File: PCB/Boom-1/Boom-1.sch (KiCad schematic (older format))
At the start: 698 parts

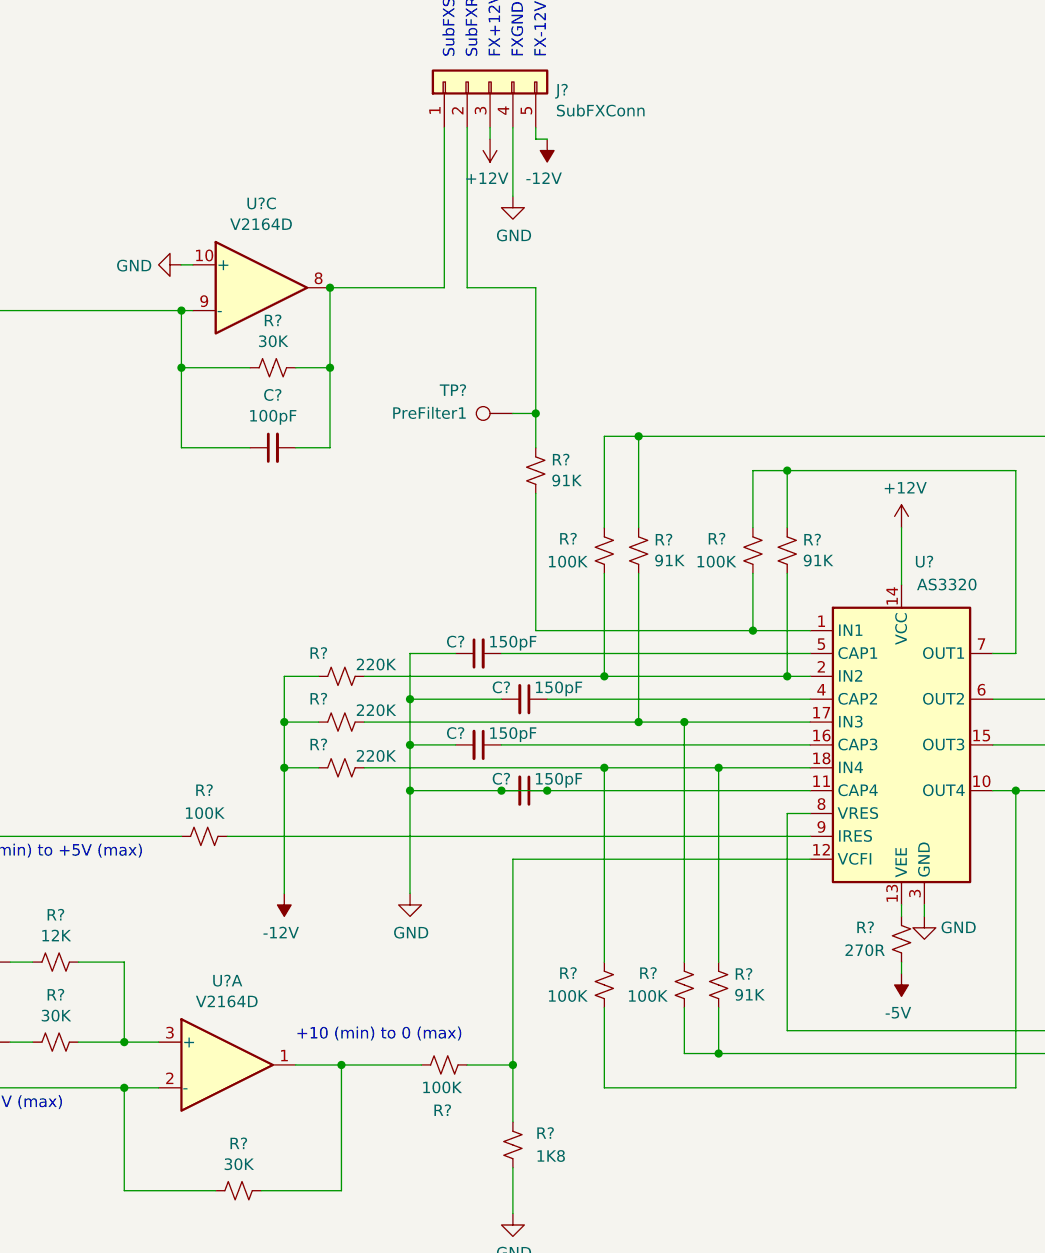
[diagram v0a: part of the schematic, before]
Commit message: replaced tl072 in sub osc filt
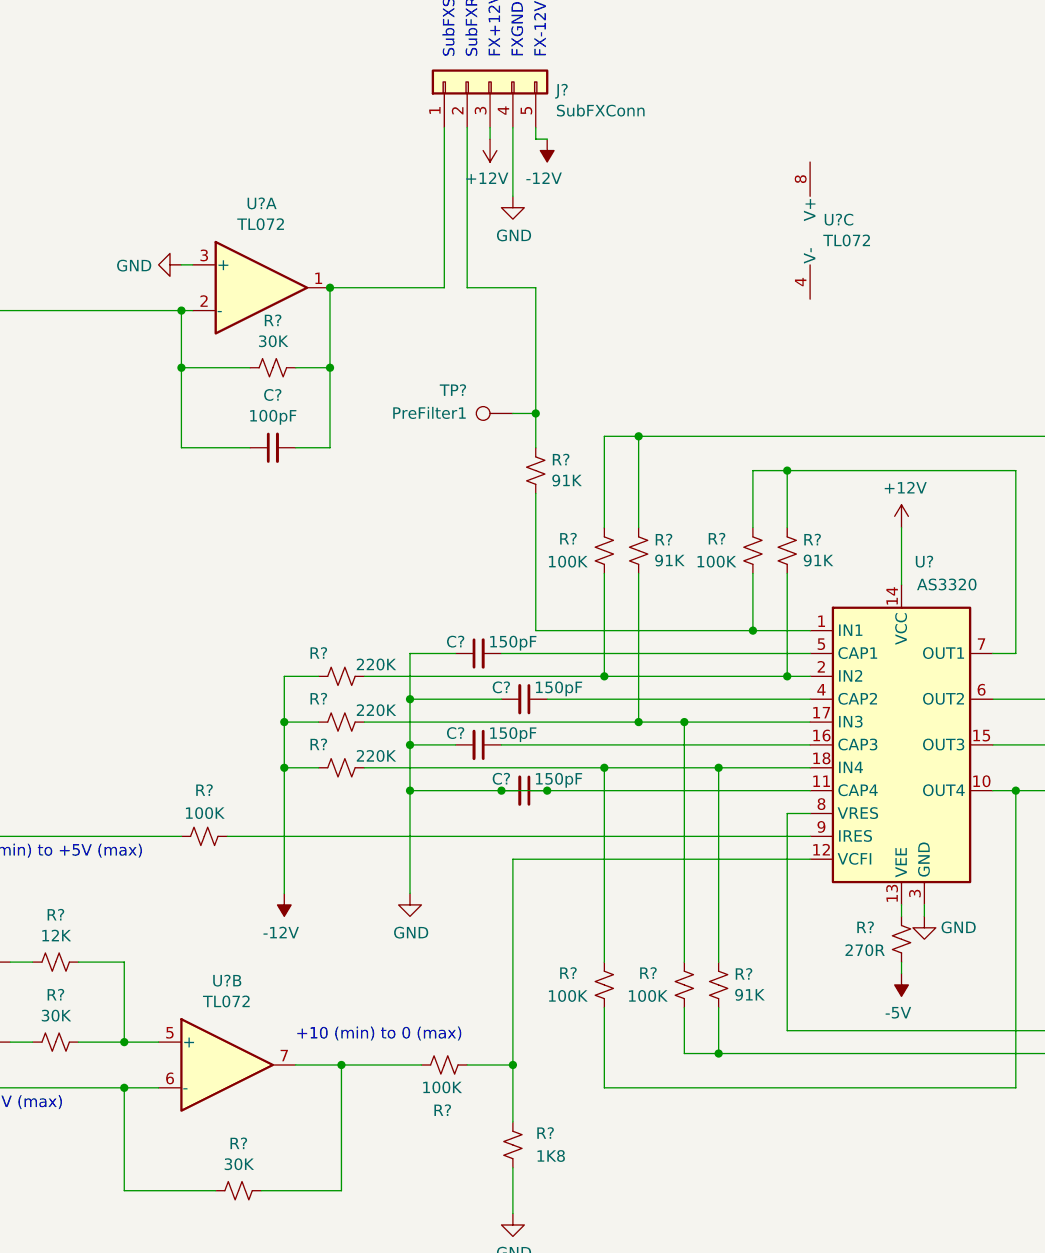
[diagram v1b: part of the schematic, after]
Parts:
- removed U? (x2): V2164D, Package_DIP:DIP-16_W7.62mm_Socket, symbol Amplifier_Operational:TL074
- added U? (x3): TL072, symbol Amplifier_Operational:TL072
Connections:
- net GND: now also U?.3 (+)
- net at C?.1, R?.2, U?.5 (Io2)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: now also U?.2 (-)
- net at C?.2, J?.1 (Pin_1), R?.1: now also U?.1
- net at R?.1, R?.2, R?.2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: now also U?.6 (-)
- net at R?.1, R?.2: now also U?.7
- net at R?.1, R?.1: now also U?.5 (+)
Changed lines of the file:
@@
 Wire Wire Line
 	22550 40500 26350 40500
-Connection ~ 18700 38300
 Wire Wire Line
 	16350 42300 16350 45400
@@
 $Comp
 L Amplifier_Operational:TL074 U?
-U 3 1 607506FD
-P 18400 38300
-F 0 "U?" H 18400 38667 50  0000 C CNN
-F 1 "V2164D" H 18400 38576 50  0000 C CNN
-F 2 "Package_DIP:DIP-16_W7.62mm_Socket" H 18350 38400 50  0001 C CNN
-F 3 "" H 18450 38500 50  0001 C CNN
-	3    18400 38300
-	1    0    0    -1
-$EndComp
-$Comp
-L Amplifier_Operational:TL074 U?
 U 1 1 5EA62AE2
 P 7100 44950
@@
 $Comp
 L Amplifier_Operational:TL074 U?
-U 1 1 6CFE24C1
-P 18250 41700
-F 0 "U?" H 18250 42067 50  0000 C CNN
-F 1 "V2164D" H 18250 41976 50  0000 C CNN
-F 2 "Package_DIP:DIP-16_W7.62mm_Socket" H 18200 41800 50  0001 C CNN
-F 3 "" H 18300 41900 50  0001 C CNN
-	1    18250 41700
-	1    0    0    -1
-$EndComp
-$Comp
-L Amplifier_Operational:TL074 U?
 U 1 1 89F24323
 P 31500 37000
@@
 	1    0    0    -1
 $EndComp
+$Comp
+L Amplifier_Operational:TL072 U?
+U 1 1 690F5BAC
+P 18400 38300
+F 0 "U?" H 18400 38667 50  0000 C CNN
+F 1 "TL072" H 18400 38576 50  0000 C CNN
+F 2 "" H 18400 38300 50  0001 C CNN
+F 3 "http://www.ti.com/lit/ds/symlink/tl071.pdf" H 18400 38300 50  0001 C CNN
+	1    18400 38300
+	1    0    0    -1
+$EndComp
+Connection ~ 18700 38300
+$Comp
+L Amplifier_Operational:TL072 U?
+U 2 1 690FE8E2
+P 18250 41700
+F 0 "U?" H 18250 42067 50  0000 C CNN
+F 1 "TL072" H 18250 41976 50  0000 C CNN
+F 2 "" H 18250 41700 50  0001 C CNN
+F 3 "http://www.ti.com/lit/ds/symlink/tl071.pdf" H 18250 41700 50  0001 C CNN
+	2    18250 41700
+	1    0    0    -1
+$EndComp
+$Comp
+L Amplifier_Operational:TL072 U?
+U 3 1 69108260
+P 20900 38050
+F 0 "U?" H 20858 38096 50  0000 L CNN
+F 1 "TL072" H 20858 38005 50  0000 L CNN
+F 2 "" H 20900 38050 50  0001 C CNN
+F 3 "http://www.ti.com/lit/ds/symlink/tl071.pdf" H 20900 38050 50  0001 C CNN
+	3    20900 38050
+	1    0    0    -1
+$EndComp

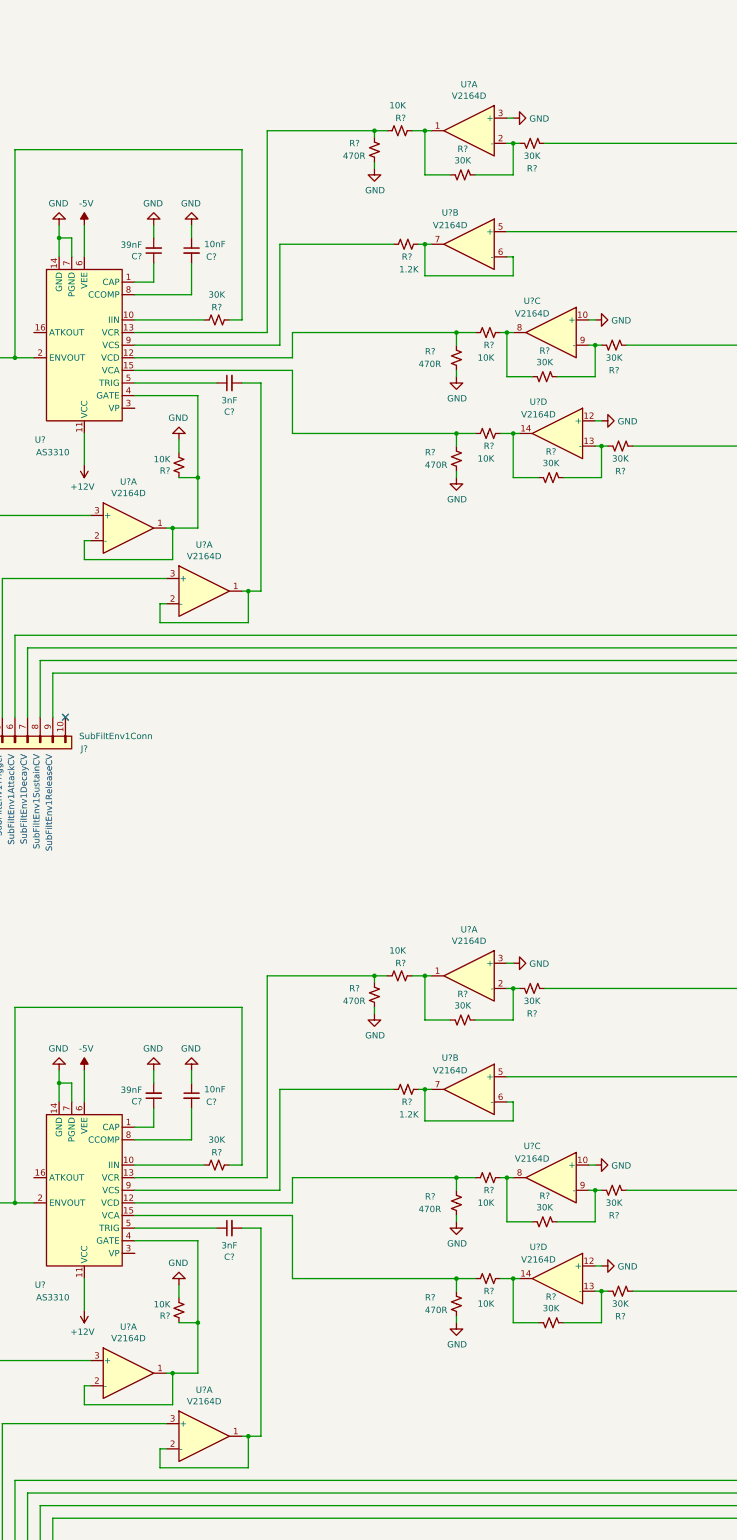
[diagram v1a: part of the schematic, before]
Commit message: replaced TL074s in sub osc filt env 1 and 2
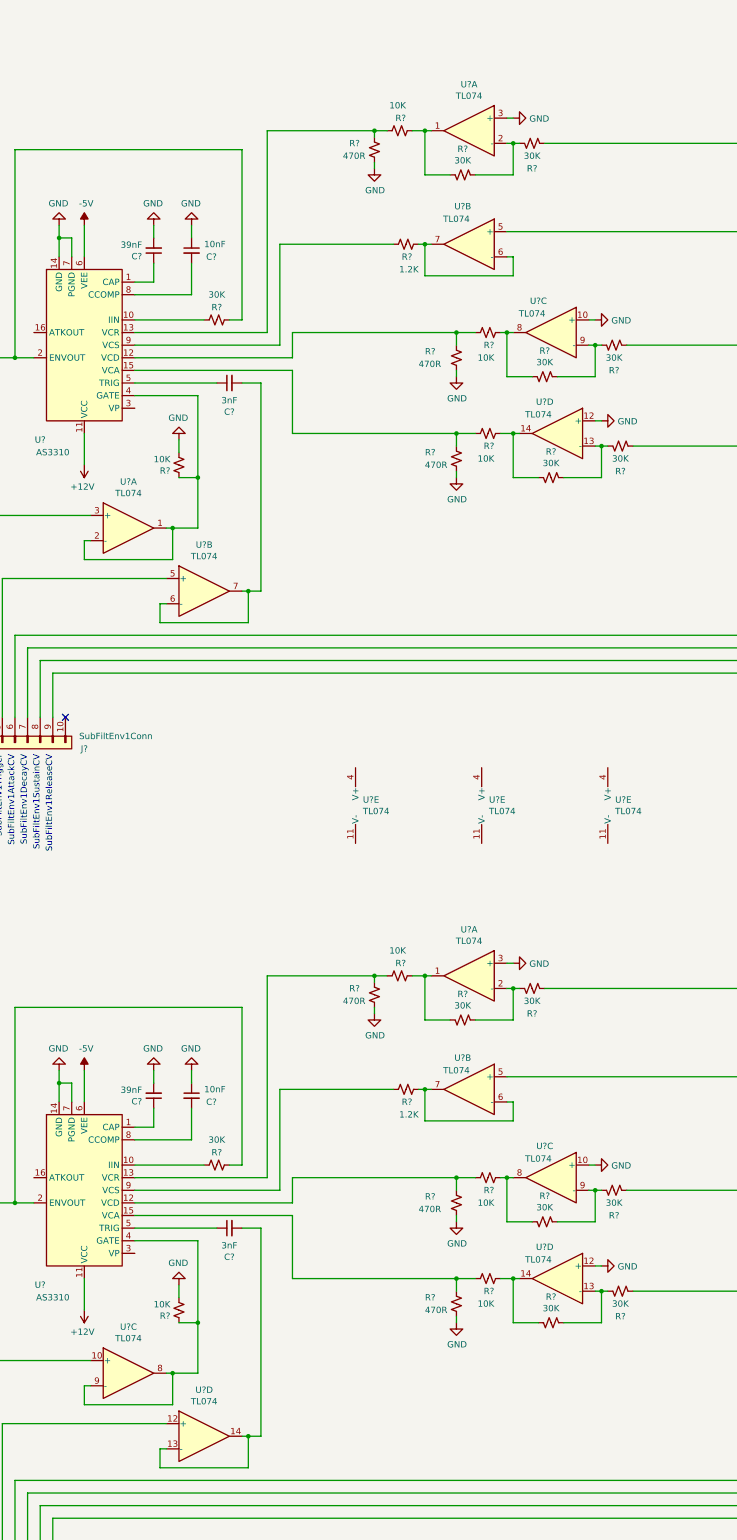
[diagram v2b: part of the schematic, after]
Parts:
- removed U? (x4): V2164D, Package_DIP:DIP-16_W7.62mm_Socket, symbol Amplifier_Operational:TL072
- removed U? (x8): V2164D, Package_DIP:DIP-16_W7.62mm_Socket, symbol Amplifier_Operational:TL074
- added U? (x15): TL074, symbol Amplifier_Operational:TL074
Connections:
- net GND: now also U?.10 (+), U?.10 (+), U?.12 (+), U?.12 (+), U?.3 (+), U?.3 (+)
- net at R?.1, U?.4 (GATE): now also U?.1, U?.2 (-)
- net at R?.1, U?.4 (GATE): now also U?.8, U?.9 (-)
- net at C?.2: now also U?.13 (-), U?.14
- net at C?.2: now also U?.6 (-), U?.7
- net at J?.4 (Pin_4): now also U?.3 (+)
- net at J?.5 (Pin_5): now also U?.5 (+)
- net at J?.4 (Pin_4): now also U?.10 (+)
- net at J?.5 (Pin_5): now also U?.12 (+)
- net at J?.8 (Pin_8): now also U?.5 (+) (x2)
- net at R?.1, R?.2: now also U?.1 (x2)
- net at R?.2: now also U?.6 (-), U?.7 (x2)
- net at R?.2, R?.2: now also U?.2 (-) (x2)
- net at R?.1, R?.2: now also U?.8 (x2)
- net at R?.2, R?.2: now also U?.9 (-) (x2)
- net at R?.1, R?.2: now also U?.14 (x2)
- net at R?.2, R?.2: now also U?.13 (-) (x2)
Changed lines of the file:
@@
 Wire Wire Line
 	22050 45700 22050 45750
-$Comp
-L Amplifier_Operational:TL074 U?
-U 2 1 8B0E7300
-P 22150 44700
-F 0 "U?" H 22300 44950 50  0000 C CNN
-F 1 "V2164D" H 22300 44850 50  0000 C CNN
-F 2 "Package_DIP:DIP-16_W7.62mm_Socket" H 22100 44800 50  0001 C CNN
-F 3 "" H 22200 44900 50  0001 C CNN
-	2    22150 44700
-	-1   0    0    -1
-$EndComp
 Wire Wire Line
 	21550 44700 20650 44700
@@
 Wire Wire Line
 	22050 52400 22050 52450
-$Comp
-L Amplifier_Operational:TL074 U?
-U 2 1 8BCFB81C
-P 22150 51400
-F 0 "U?" H 22300 51650 50  0000 C CNN
-F 1 "V2164D" H 22300 51550 50  0000 C CNN
-F 2 "Package_DIP:DIP-16_W7.62mm_Socket" H 22100 51500 50  0001 C CNN
-F 3 "" H 22200 51600 50  0001 C CNN
-	2    22150 51400
-	-1   0    0    -1
-$EndComp
 Wire Wire Line
 	21550 51400 20650 51400
@@
 $Comp
 L Amplifier_Operational:TL074 U?
-U 1 1 8B0E705B
-P 22150 43800
-F 0 "U?" H 22150 44167 50  0000 C CNN
-F 1 "V2164D" H 22150 44076 50  0000 C CNN
-F 2 "Package_DIP:DIP-16_W7.62mm_Socket" H 22100 43900 50  0001 C CNN
-F 3 "" H 22200 44000 50  0001 C CNN
-	1    22150 43800
-	-1   0    0    -1
-$EndComp
-$Comp
-L Amplifier_Operational:TL074 U?
-U 3 1 8B0E7151
-P 22800 45400
-F 0 "U?" H 22950 45650 50  0000 C CNN
-F 1 "V2164D" H 22950 45550 50  0000 C CNN
-F 2 "Package_DIP:DIP-16_W7.62mm_Socket" H 22750 45500 50  0001 C CNN
-F 3 "" H 22850 45600 50  0001 C CNN
-	3    22800 45400
-	-1   0    0    -1
-$EndComp
-$Comp
-L Amplifier_Operational:TL074 U?
-U 4 1 8B0E7247
-P 22850 46200
-F 0 "U?" H 23000 46450 50  0000 C CNN
-F 1 "V2164D" H 23000 46350 50  0000 C CNN
-F 2 "Package_DIP:DIP-16_W7.62mm_Socket" H 22800 46300 50  0001 C CNN
-F 3 "" H 22900 46400 50  0001 C CNN
-	4    22850 46200
-	-1   0    0    -1
-$EndComp
-$Comp
-L Amplifier_Operational:TL074 U?
-U 1 1 8BCFB577
-P 22150 50500
-F 0 "U?" H 22150 50867 50  0000 C CNN
-F 1 "V2164D" H 22150 50776 50  0000 C CNN
-F 2 "Package_DIP:DIP-16_W7.62mm_Socket" H 22100 50600 50  0001 C CNN
-F 3 "" H 22200 50700 50  0001 C CNN
-	1    22150 50500
-	-1   0    0    -1
-$EndComp
-$Comp
-L Amplifier_Operational:TL074 U?
-U 3 1 8BCFB66D
-P 22800 52100
-F 0 "U?" H 22950 52350 50  0000 C CNN
-F 1 "V2164D" H 22950 52250 50  0000 C CNN
-F 2 "Package_DIP:DIP-16_W7.62mm_Socket" H 22750 52200 50  0001 C CNN
-F 3 "" H 22850 52300 50  0001 C CNN
-	3    22800 52100
-	-1   0    0    -1
-$EndComp
-$Comp
-L Amplifier_Operational:TL074 U?
-U 4 1 8BCFB763
-P 22850 52900
-F 0 "U?" H 23000 53150 50  0000 C CNN
-F 1 "V2164D" H 23000 53050 50  0000 C CNN
-F 2 "Package_DIP:DIP-16_W7.62mm_Socket" H 22800 53000 50  0001 C CNN
-F 3 "" H 22900 53100 50  0001 C CNN
-	4    22850 52900
-	-1   0    0    -1
-$EndComp
-$Comp
-L Amplifier_Operational:TL074 U?
 U 1 1 65B745CD
 P 27950 35850
@@
 $Comp
 L Amplifier_Operational:TL072 U?
-U 1 1 6F3C43BC
-P 19450 46950
-F 0 "U?" H 19450 47317 50  0000 C CNN
-F 1 "V2164D" H 19450 47226 50  0000 C CNN
-F 2 "Package_DIP:DIP-16_W7.62mm_Socket" H 19450 46950 50  0001 C CNN
-F 3 "" H 19450 46950 50  0001 C CNN
-	1    19450 46950
-	1    0    0    -1
-$EndComp
-$Comp
-L Amplifier_Operational:TL072 U?
-U 1 1 6F3C4461
-P 20050 47450
-F 0 "U?" H 20050 47817 50  0000 C CNN
-F 1 "V2164D" H 20050 47726 50  0000 C CNN
-F 2 "Package_DIP:DIP-16_W7.62mm_Socket" H 20050 47450 50  0001 C CNN
-F 3 "" H 20050 47450 50  0001 C CNN
-	1    20050 47450
-	1    0    0    -1
-$EndComp
-$Comp
-L Amplifier_Operational:TL072 U?
-U 1 1 6F9DDD6A
-P 19450 53650
-F 0 "U?" H 19450 54017 50  0000 C CNN
-F 1 "V2164D" H 19450 53926 50  0000 C CNN
-F 2 "Package_DIP:DIP-16_W7.62mm_Socket" H 19450 53650 50  0001 C CNN
-F 3 "" H 19450 53650 50  0001 C CNN
-	1    19450 53650
-	1    0    0    -1
-$EndComp
-$Comp
-L Amplifier_Operational:TL072 U?
-U 1 1 6F9DDE0F
-P 20050 54150
-F 0 "U?" H 20050 54517 50  0000 C CNN
-F 1 "V2164D" H 20050 54426 50  0000 C CNN
-F 2 "Package_DIP:DIP-16_W7.62mm_Socket" H 20050 54150 50  0001 C CNN
-F 3 "" H 20050 54150 50  0001 C CNN
-	1    20050 54150
-	1    0    0    -1
-$EndComp
-$Comp
-L Amplifier_Operational:TL072 U?
 U 1 1 72B40446
 P 28800 40150
@@
 	1    0    0    -1
 $EndComp
+$Comp
+L Amplifier_Operational:TL074 U?
+U 1 1 69118965
+P 22150 43800
+F 0 "U?" H 22150 44167 50  0000 C CNN
+F 1 "TL074" H 22150 44076 50  0000 C CNN
+F 2 "" H 22100 43900 50  0001 C CNN
+F 3 "http://www.ti.com/lit/ds/symlink/tl071.pdf" H 22200 44000 50  0001 C CNN
+	1    22150 43800
+	-1   0    0    -1
+$EndComp
+$Comp
+L Amplifier_Operational:TL074 U?
+U 2 1 69122BD1
+P 22150 44700
+F 0 "U?" H 22200 45000 50  0000 C CNN
+F 1 "TL074" H 22250 44900 50  0000 C CNN
+F 2 "" H 22100 44800 50  0001 C CNN
+F 3 "http://www.ti.com/lit/ds/symlink/tl071.pdf" H 22200 44900 50  0001 C CNN
+	2    22150 44700
+	-1   0    0    -1
+$EndComp
+$Comp
+L Amplifier_Operational:TL074 U?
+U 3 1 6912A75B
+P 22800 45400
+F 0 "U?" H 22900 45650 50  0000 C CNN
+F 1 "TL074" H 22950 45550 50  0000 C CNN
+F 2 "" H 22750 45500 50  0001 C CNN
+F 3 "http://www.ti.com/lit/ds/symlink/tl071.pdf" H 22850 45600 50  0001 C CNN
+	3    22800 45400
+	-1   0    0    -1
+$EndComp
+$Comp
+L Amplifier_Operational:TL074 U?
+U 4 1 69132469
+P 22850 46200
+F 0 "U?" H 22950 46450 50  0000 C CNN
+F 1 "TL074" H 23000 46350 50  0000 C CNN
+F 2 "" H 22800 46300 50  0001 C CNN
+F 3 "http://www.ti.com/lit/ds/symlink/tl071.pdf" H 22900 46400 50  0001 C CNN
+	4    22850 46200
+	-1   0    0    -1
+$EndComp
+$Comp
+L Amplifier_Operational:TL074 U?
+U 1 1 6913BED9
+P 19450 46950
+F 0 "U?" H 19450 47317 50  0000 C CNN
+F 1 "TL074" H 19450 47226 50  0000 C CNN
+F 2 "" H 19400 47050 50  0001 C CNN
+F 3 "http://www.ti.com/lit/ds/symlink/tl071.pdf" H 19500 47150 50  0001 C CNN
+	1    19450 46950
+	1    0    0    -1
+$EndComp
+$Comp
+L Amplifier_Operational:TL074 U?
+U 2 1 69143B65
+P 20050 47450
+F 0 "U?" H 20050 47817 50  0000 C CNN
+F 1 "TL074" H 20050 47726 50  0000 C CNN
+F 2 "" H 20000 47550 50  0001 C CNN
+F 3 "http://www.ti.com/lit/ds/symlink/tl071.pdf" H 20100 47650 50  0001 C CNN
+	2    20050 47450
+	1    0    0    -1
+$EndComp
+$Comp
+L Amplifier_Operational:TL074 U?
+U 3 1 6914B6F3
+P 19450 53650
+F 0 "U?" H 19450 54017 50  0000 C CNN
+F 1 "TL074" H 19450 53926 50  0000 C CNN
+F 2 "" H 19400 53750 50  0001 C CNN
+F 3 "http://www.ti.com/lit/ds/symlink/tl071.pdf" H 19500 53850 50  0001 C CNN
+	3    19450 53650
+	1    0    0    -1
+$EndComp
+$Comp
+L Amplifier_Operational:TL074 U?
+U 4 1 6915280A
+P 20050 54150
+F 0 "U?" H 20050 54517 50  0000 C CNN
+F 1 "TL074" H 20050 54426 50  0000 C CNN
+F 2 "" H 20000 54250 50  0001 C CNN
+F 3 "http://www.ti.com/lit/ds/symlink/tl071.pdf" H 20100 54350 50  0001 C CNN
+	4    20050 54150
+	1    0    0    -1
+$EndComp
+$Comp
+L Amplifier_Operational:TL074 U?
+U 1 1 6915A9DD
+P 22150 50500
+F 0 "U?" H 22150 50867 50  0000 C CNN
+F 1 "TL074" H 22150 50776 50  0000 C CNN
+F 2 "" H 22100 50600 50  0001 C CNN
+F 3 "http://www.ti.com/lit/ds/symlink/tl071.pdf" H 22200 50700 50  0001 C CNN
+	1    22150 50500
+	-1   0    0    -1
+$EndComp
+$Comp
+L Amplifier_Operational:TL074 U?
+U 2 1 6916277F
+P 22150 51400
+F 0 "U?" H 22200 51650 50  0000 C CNN
+F 1 "TL074" H 22250 51550 50  0000 C CNN
+F 2 "" H 22100 51500 50  0001 C CNN
+F 3 "http://www.ti.com/lit/ds/symlink/tl071.pdf" H 22200 51600 50  0001 C CNN
+	2    22150 51400
+	-1   0    0    -1
+$EndComp
+$Comp
+L Amplifier_Operational:TL074 U?
+U 3 1 6916A582
+P 22800 52100
+F 0 "U?" H 22850 52350 50  0000 C CNN
+F 1 "TL074" H 22900 52250 50  0000 C CNN
+F 2 "" H 22750 52200 50  0001 C CNN
+F 3 "http://www.ti.com/lit/ds/symlink/tl071.pdf" H 22850 52300 50  0001 C CNN
+	3    22800 52100
+	-1   0    0    -1
+$EndComp
+$Comp
+L Amplifier_Operational:TL074 U?
+U 4 1 69171A0C
+P 22850 52900
+F 0 "U?" H 22950 53150 50  0000 C CNN
+F 1 "TL074" H 23000 53050 50  0000 C CNN
+F 2 "" H 22800 53000 50  0001 C CNN
+F 3 "http://www.ti.com/lit/ds/symlink/tl071.pdf" H 22900 53100 50  0001 C CNN
+	4    22850 52900
+	-1   0    0    -1
+$EndComp
+$Comp
+L Amplifier_Operational:TL074 U?
+U 5 1 6917B785
+P 21350 49150
+F 0 "U?" H 21308 49196 50  0000 L CNN
+F 1 "TL074" H 21308 49105 50  0000 L CNN
+F 2 "" H 21300 49250 50  0001 C CNN
+F 3 "http://www.ti.com/lit/ds/symlink/tl071.pdf" H 21400 49350 50  0001 C CNN
+	5    21350 49150
+	1    0    0    -1
+$EndComp
+$Comp
+L Amplifier_Operational:TL074 U?
+U 5 1 69181953
+P 22350 49150
+F 0 "U?" H 22308 49196 50  0000 L CNN
+F 1 "TL074" H 22308 49105 50  0000 L CNN
+F 2 "" H 22300 49250 50  0001 C CNN
+F 3 "http://www.ti.com/lit/ds/symlink/tl071.pdf" H 22400 49350 50  0001 C CNN
+	5    22350 49150
+	1    0    0    -1
+$EndComp
+$Comp
+L Amplifier_Operational:TL074 U?
+U 5 1 69183854
+P 23350 49150
+F 0 "U?" H 23308 49196 50  0000 L CNN
+F 1 "TL074" H 23308 49105 50  0000 L CNN
+F 2 "" H 23300 49250 50  0001 C CNN
+F 3 "http://www.ti.com/lit/ds/symlink/tl071.pdf" H 23400 49350 50  0001 C CNN
+	5    23350 49150
+	1    0    0    -1
+$EndComp
